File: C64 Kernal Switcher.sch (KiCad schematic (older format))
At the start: 11 parts, among them J1 Signals, J2 RGB, J3 LED, U1 2364, U2 PIC12F629-I/MS, U3 27C256

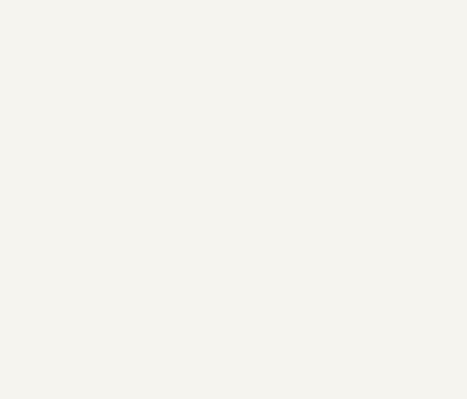
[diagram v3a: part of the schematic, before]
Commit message: Assigned footprints
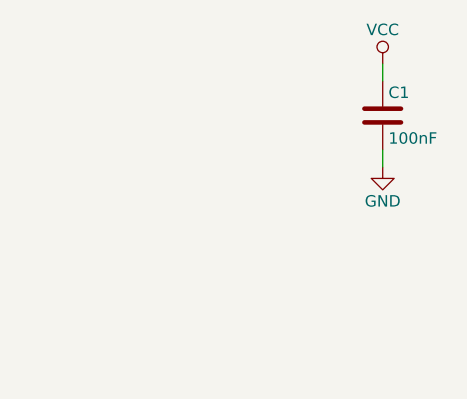
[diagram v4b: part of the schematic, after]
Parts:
- added C1: 100nF, Capacitors_THT:C_Disc_D4.7mm_W2.5mm_P5.00mm, symbol C
- J1: footprint (none) -> Pin_Headers:Pin_Header_Angled_1x02_Pitch2.54mm
- J2: footprint (none) -> Pin_Headers:Pin_Header_Straight_2x03_Pitch2.54mm
- U2: footprint (none) -> Housings_DIP:DIP-8_W7.62mm_Socket
- U3: footprint (none) -> Housings_DIP:DIP-28_W15.24mm_Socket_LongPads
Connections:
- net GND: now also C1.2
- net VCC: now also C1.1
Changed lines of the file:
@@
 	6075 2575 6175 2675
 $Comp
-L VCC #PWR01
+L VCC #PWR5
 U 1 1 5CC71BAE
 P 3900 3375
-F 0 "#PWR01" H 3900 3225 50  0001 C CNN
+F 0 "#PWR5" H 3900 3225 50  0001 C CNN
 F 1 "VCC" H 3900 3525 50  0000 C CNN
 F 2 "" H 3900 3375 50  0001 C CNN
@@
 CS
 $Comp
-L VCC #PWR02
+L VCC #PWR3
 U 1 1 5CC72126
 P 2700 1525
-F 0 "#PWR02" H 2700 1375 50  0001 C CNN
+F 0 "#PWR3" H 2700 1375 50  0001 C CNN
 F 1 "VCC" H 2700 1675 50  0000 C CNN
 F 2 "" H 2700 1525 50  0001 C CNN
@@
 $EndComp
 $Comp
-L GND #PWR03
+L GND #PWR4
 U 1 1 5CC72179
 P 2700 4025
-F 0 "#PWR03" H 2700 3775 50  0001 C CNN
+F 0 "#PWR4" H 2700 3775 50  0001 C CNN
 F 1 "GND" H 2700 3875 50  0000 C CNN
 F 2 "" H 2700 4025 50  0001 C CNN
@@
 $EndComp
 $Comp
-L VCC #PWR04
+L VCC #PWR8
 U 1 1 5CC72A38
 P 6875 1375
-F 0 "#PWR04" H 6875 1225 50  0001 C CNN
+F 0 "#PWR8" H 6875 1225 50  0001 C CNN
 F 1 "VCC" H 6875 1525 50  0000 C CNN
 F 2 "" H 6875 1375 50  0001 C CNN
@@
 $EndComp
 $Comp
-L GND #PWR05
+L GND #PWR9
 U 1 1 5CC72A4C
 P 6875 1875
-F 0 "#PWR05" H 6875 1625 50  0001 C CNN
+F 0 "#PWR9" H 6875 1625 50  0001 C CNN
 F 1 "GND" H 6875 1725 50  0000 C CNN
 F 2 "" H 6875 1875 50  0001 C CNN
@@
 $EndComp
 $Comp
-L VCC #PWR06
+L VCC #PWR10
 U 1 1 5CC72AB2
 P 7150 1950
-F 0 "#PWR06" H 7150 1800 50  0001 C CNN
+F 0 "#PWR10" H 7150 1800 50  0001 C CNN
 F 1 "VCC" H 7150 2100 50  0000 C CNN
 F 2 "" H 7150 1950 50  0001 C CNN
@@
 $EndComp
 $Comp
-L GND #PWR07
+L GND #PWR11
 U 1 1 5CC72AB8
 P 7150 2450
-F 0 "#PWR07" H 7150 2200 50  0001 C CNN
+F 0 "#PWR11" H 7150 2200 50  0001 C CNN
 F 1 "GND" H 7150 2300 50  0000 C CNN
 F 2 "" H 7150 2450 50  0001 C CNN
@@
 	6275 4950 6475 4950
 $Comp
-L GND #PWR08
+L GND #PWR7
 U 1 1 5CC74328
 P 6375 5050
-F 0 "#PWR08" H 6375 4800 50  0001 C CNN
+F 0 "#PWR7" H 6375 4800 50  0001 C CNN
 F 1 "GND" H 6375 4900 50  0000 C CNN
 F 2 "" H 6375 5050 50  0001 C CNN
@@
 F 0 "U2" H 2000 6300 50  0000 L CNN
 F 1 "PIC12F629-I/MS" H 2000 6200 50  0000 L CNN
-F 2 "" H 2550 5750 50  0001 C CNN
+F 2 "Housings_DIP:DIP-8_W7.62mm_Socket" H 2550 5750 50  0001 C CNN
 F 3 "" H 2550 5750 50  0001 C CNN
 	1    2550 5750
@@
 $EndComp
 $Comp
-L VCC #PWR09
+L VCC #PWR1
 U 1 1 5D07A987
 P 1775 5375
-F 0 "#PWR09" H 1775 5225 50  0001 C CNN
+F 0 "#PWR1" H 1775 5225 50  0001 C CNN
 F 1 "VCC" H 1775 5525 50  0000 C CNN
 F 2 "" H 1775 5375 50  0001 C CNN
@@
 	1775 5450 1850 5450
 $Comp
-L GND #PWR010
+L GND #PWR2
 U 1 1 5D07AAD6
 P 1775 6125
-F 0 "#PWR010" H 1775 5875 50  0001 C CNN
+F 0 "#PWR2" H 1775 5875 50  0001 C CNN
 F 1 "GND" H 1775 5975 50  0000 C CNN
 F 2 "" H 1775 6125 50  0001 C CNN
@@
 F 0 "U3" H 4975 3775 50  0000 C CNN
 F 1 "27C256" H 5125 1775 50  0000 C CNN
-F 2 "" H 5125 2775 50  0001 C CNN
+F 2 "Housings_DIP:DIP-28_W15.24mm_Socket_LongPads" H 5125 2775 50  0001 C CNN
 F 3 "" H 5125 2775 50  0001 C CNN
 	1    5125 2775
@@
 F 0 "J2" H 6675 5750 50  0000 C CNN
 F 1 "RGB" H 6675 5350 50  0000 C CNN
-F 2 "" H 6625 5550 50  0001 C CNN
+F 2 "Pin_Headers:Pin_Header_Straight_2x03_Pitch2.54mm" H 6625 5550 50  0001 C CNN
 F 3 "" H 6625 5550 50  0001 C CNN
 	1    6625 5550
@@
 NoConn ~ 6425 5650
 $Comp
-L GND #PWR011
+L GND #PWR12
 U 1 1 5D07DC30
 P 7350 5625
-F 0 "#PWR011" H 7350 5375 50  0001 C CNN
+F 0 "#PWR12" H 7350 5375 50  0001 C CNN
 F 1 "GND" H 7350 5475 50  0000 C CNN
 F 2 "" H 7350 5625 50  0001 C CNN
@@
 	7350 5550 6925 5550
 $Comp
-L GND #PWR012
+L GND #PWR6
 U 1 1 5D07DCBB
 P 6300 5625
-F 0 "#PWR012" H 6300 5375 50  0001 C CNN
+F 0 "#PWR6" H 6300 5375 50  0001 C CNN
 F 1 "GND" H 6300 5475 50  0000 C CNN
 F 2 "" H 6300 5625 50  0001 C CNN
@@
 F 0 "J1" H 6675 4275 50  0000 C CNN
 F 1 "Signals" H 6675 3975 50  0000 C CNN
-F 2 "" H 6675 4175 50  0001 C CNN
+F 2 "Pin_Headers:Pin_Header_Angled_1x02_Pitch2.54mm" H 6675 4175 50  0001 C CNN
 F 3 "" H 6675 4175 50  0001 C CNN
 	1    6675 4175
@@
 Text GLabel 6400 4275 0    60   BiDi ~ 0
 ~RESET
+$Comp
+L C C1
+U 1 1 5D07F04A
+P 10300 950
+F 0 "C1" H 10325 1050 50  0000 L CNN
+F 1 "100nF" H 10325 850 50  0000 L CNN
+F 2 "Capacitors_THT:C_Disc_D4.7mm_W2.5mm_P5.00mm" H 10338 800 50  0001 C CNN
+F 3 "" H 10300 950 50  0001 C CNN
+	1    10300 950
+	1    0    0    -1
+$EndComp
+$Comp
+L VCC #PWR13
+U 1 1 5D07F12B
+P 10300 725
+F 0 "#PWR13" H 10300 575 50  0001 C CNN
+F 1 "VCC" H 10300 875 50  0000 C CNN
+F 2 "" H 10300 725 50  0001 C CNN
+F 3 "" H 10300 725 50  0001 C CNN
+	1    10300 725
+	1    0    0    -1
+$EndComp
+$Comp
+L GND #PWR14
+U 1 1 5D07F1EA
+P 10300 1175
+F 0 "#PWR14" H 10300 925 50  0001 C CNN
+F 1 "GND" H 10300 1025 50  0000 C CNN
+F 2 "" H 10300 1175 50  0001 C CNN
+F 3 "" H 10300 1175 50  0001 C CNN
+	1    10300 1175
+	1    0    0    -1
+$EndComp
+Wire Wire Line
+	10300 1175 10300 1100
+Wire Wire Line
+	10300 800  10300 725
 $EndSCHEMATC

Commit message: Layout redone
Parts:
- J3: footprint Pin_Headers:Pin_Header_Straight_1x03_Pitch2.54mm -> Pin_Headers:Pin_Header_Angled_1x03_Pitch2.54mm
- U1: footprint Housings_DIP:DIP-24_W15.24mm_Socket -> 2364:DIP-24_W15.24mm_Socket
- U3: footprint Housings_DIP:DIP-28_W15.24mm_Socket_LongPads -> Housings_DIP:DIP-28_W15.24mm_Socket
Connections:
- net CS: no longer U3.20 (CE)
- net GND: now also U3.20 (CE)
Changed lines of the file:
@@
 F 0 "U1" H 2900 3775 50  0000 C CNN
 F 1 "2364" H 3000 1775 50  0000 C CNN
-F 2 "Housings_DIP:DIP-24_W15.24mm_Socket" H 2700 2775 50  0001 C CNN
+F 2 "2364:DIP-24_W15.24mm_Socket" H 2700 2775 50  0001 C CNN
 F 3 "" H 2700 2775 50  0001 C CNN
 	1    2700 2775
@@
 	4075 2975 4175 3075
 Entry Wire Line
-	4075 3475 4175 3575
+	4075 3575 4175 3675
 Text Label 4400 3175 2    60   ~ 0
 A13
@@
 	6075 2575 6175 2675
 $Comp
-L VCC #PWR5
+L VCC #PWR01
 U 1 1 5CC71BAE
 P 3900 3375
-F 0 "#PWR5" H 3900 3225 50  0001 C CNN
+F 0 "#PWR01" H 3900 3225 50  0001 C CNN
 F 1 "VCC" H 3900 3525 50  0000 C CNN
 F 2 "" H 3900 3375 50  0001 C CNN
@@
 Text Label 1975 3675 2    60   ~ 0
 CS
-Text Label 4200 3575 0    60   ~ 0
+Text Label 4225 3675 0    60   ~ 0
 CS
 $Comp
-L VCC #PWR3
+L VCC #PWR02
 U 1 1 5CC72126
 P 2700 1525
-F 0 "#PWR3" H 2700 1375 50  0001 C CNN
+F 0 "#PWR02" H 2700 1375 50  0001 C CNN
 F 1 "VCC" H 2700 1675 50  0000 C CNN
 F 2 "" H 2700 1525 50  0001 C CNN
@@
 $EndComp
 $Comp
-L GND #PWR4
+L GND #PWR03
 U 1 1 5CC72179
 P 2700 4025
-F 0 "#PWR4" H 2700 3775 50  0001 C CNN
+F 0 "#PWR03" H 2700 3775 50  0001 C CNN
 F 1 "GND" H 2700 3875 50  0000 C CNN
 F 2 "" H 2700 4025 50  0001 C CNN
@@
 $EndComp
 $Comp
-L VCC #PWR8
+L VCC #PWR04
 U 1 1 5CC72A38
 P 6875 1375
-F 0 "#PWR8" H 6875 1225 50  0001 C CNN
+F 0 "#PWR04" H 6875 1225 50  0001 C CNN
 F 1 "VCC" H 6875 1525 50  0000 C CNN
 F 2 "" H 6875 1375 50  0001 C CNN
@@
 $EndComp
 $Comp
-L GND #PWR9
+L GND #PWR05
 U 1 1 5CC72A4C
 P 6875 1875
-F 0 "#PWR9" H 6875 1625 50  0001 C CNN
+F 0 "#PWR05" H 6875 1625 50  0001 C CNN
 F 1 "GND" H 6875 1725 50  0000 C CNN
 F 2 "" H 6875 1875 50  0001 C CNN
@@
 $EndComp
 $Comp
-L VCC #PWR10
+L VCC #PWR06
 U 1 1 5CC72AB2
 P 7150 1950
-F 0 "#PWR10" H 7150 1800 50  0001 C CNN
+F 0 "#PWR06" H 7150 1800 50  0001 C CNN
 F 1 "VCC" H 7150 2100 50  0000 C CNN
 F 2 "" H 7150 1950 50  0001 C CNN
@@
 $EndComp
 $Comp
-L GND #PWR11
+L GND #PWR07
 U 1 1 5CC72AB8
 P 7150 2450
-F 0 "#PWR11" H 7150 2200 50  0001 C CNN
+F 0 "#PWR07" H 7150 2200 50  0001 C CNN
 F 1 "GND" H 7150 2300 50  0000 C CNN
 F 2 "" H 7150 2450 50  0001 C CNN
@@
 Wire Wire Line
 	4175 3075 4425 3075
-Wire Wire Line
-	4175 3575 4425 3575
 Wire Wire Line
 	4175 3175 4425 3175
@@
 	3750 1050 3750 2675
 Wire Bus Line
-	4075 1050 4075 3475
+	4075 1050 4075 3575
 Wire Bus Line
 	6175 1050 6175 2675
@@
 	6275 2200 7050 2200
 Wire Wire Line
-	4425 3675 4350 3675
-Wire Wire Line
-	4350 3675 4350 3575
-Connection ~ 4350 3575
+	4175 3675 4425 3675
 Text GLabel 6650 1700 3    60   Input ~ 0
 A13
@@
 	6275 4950 6475 4950
 $Comp
-L GND #PWR7
+L GND #PWR08
 U 1 1 5CC74328
 P 6375 5050
-F 0 "#PWR7" H 6375 4800 50  0001 C CNN
+F 0 "#PWR08" H 6375 4800 50  0001 C CNN
 F 1 "GND" H 6375 4900 50  0000 C CNN
 F 2 "" H 6375 5050 50  0001 C CNN
@@
 F 0 "J3" H 6675 5050 50  0000 C CNN
 F 1 "LED" H 6675 4650 50  0000 C CNN
-F 2 "Pin_Headers:Pin_Header_Straight_1x03_Pitch2.54mm" H 6675 4850 50  0001 C CNN
+F 2 "Pin_Headers:Pin_Header_Angled_1x03_Pitch2.54mm" H 6675 4850 50  0001 C CNN
 F 3 "" H 6675 4850 50  0001 C CNN
 	1    6675 4850
@@
 $EndComp
 $Comp
-L VCC #PWR1
+L VCC #PWR09
 U 1 1 5D07A987
 P 1775 5375
-F 0 "#PWR1" H 1775 5225 50  0001 C CNN
+F 0 "#PWR09" H 1775 5225 50  0001 C CNN
 F 1 "VCC" H 1775 5525 50  0000 C CNN
 F 2 "" H 1775 5375 50  0001 C CNN
@@
 	1775 5450 1850 5450
 $Comp
-L GND #PWR2
+L GND #PWR010
 U 1 1 5D07AAD6
 P 1775 6125
-F 0 "#PWR2" H 1775 5875 50  0001 C CNN
+F 0 "#PWR010" H 1775 5875 50  0001 C CNN
 F 1 "GND" H 1775 5975 50  0000 C CNN
 F 2 "" H 1775 6125 50  0001 C CNN
@@
 F 0 "U3" H 4975 3775 50  0000 C CNN
 F 1 "27C256" H 5125 1775 50  0000 C CNN
-F 2 "Housings_DIP:DIP-28_W15.24mm_Socket_LongPads" H 5125 2775 50  0001 C CNN
+F 2 "Housings_DIP:DIP-28_W15.24mm_Socket" H 5125 2775 50  0001 C CNN
 F 3 "" H 5125 2775 50  0001 C CNN
 	1    5125 2775
@@
 NoConn ~ 6425 5650
 $Comp
-L GND #PWR12
+L GND #PWR011
 U 1 1 5D07DC30
 P 7350 5625
-F 0 "#PWR12" H 7350 5375 50  0001 C CNN
+F 0 "#PWR011" H 7350 5375 50  0001 C CNN
 F 1 "GND" H 7350 5475 50  0000 C CNN
 F 2 "" H 7350 5625 50  0001 C CNN
@@
 	7350 5550 6925 5550
 $Comp
-L GND #PWR6
+L GND #PWR012
 U 1 1 5D07DCBB
 P 6300 5625
-F 0 "#PWR6" H 6300 5375 50  0001 C CNN
+F 0 "#PWR012" H 6300 5375 50  0001 C CNN
 F 1 "GND" H 6300 5475 50  0000 C CNN
 F 2 "" H 6300 5625 50  0001 C CNN
@@
 $EndComp
 $Comp
-L VCC #PWR13
+L VCC #PWR013
 U 1 1 5D07F12B
 P 10300 725
-F 0 "#PWR13" H 10300 575 50  0001 C CNN
+F 0 "#PWR013" H 10300 575 50  0001 C CNN
 F 1 "VCC" H 10300 875 50  0000 C CNN
 F 2 "" H 10300 725 50  0001 C CNN
@@
 $EndComp
 $Comp
-L GND #PWR14
+L GND #PWR014
 U 1 1 5D07F1EA
 P 10300 1175
-F 0 "#PWR14" H 10300 925 50  0001 C CNN
+F 0 "#PWR014" H 10300 925 50  0001 C CNN
 F 1 "GND" H 10300 1025 50  0000 C CNN
 F 2 "" H 10300 1175 50  0001 C CNN
@@
 Wire Wire Line
 	10300 800  10300 725
+$Comp
+L GND #PWR?
+U 1 1 5D07DD0A
+P 3900 3500
+F 0 "#PWR?" H 3900 3250 50  0001 C CNN
+F 1 "GND" H 3900 3350 50  0000 C CNN
+F 2 "" H 3900 3500 50  0001 C CNN
+F 3 "" H 3900 3500 50  0001 C CNN
+	1    3900 3500
+	1    0    0    -1
+$EndComp
+Wire Wire Line
+	3900 3425 3900 3500
+Wire Wire Line
+	3900 3425 4350 3425
+Wire Wire Line
+	4350 3425 4350 3575
+Wire Wire Line
+	4350 3575 4425 3575
 $EndSCHEMATC

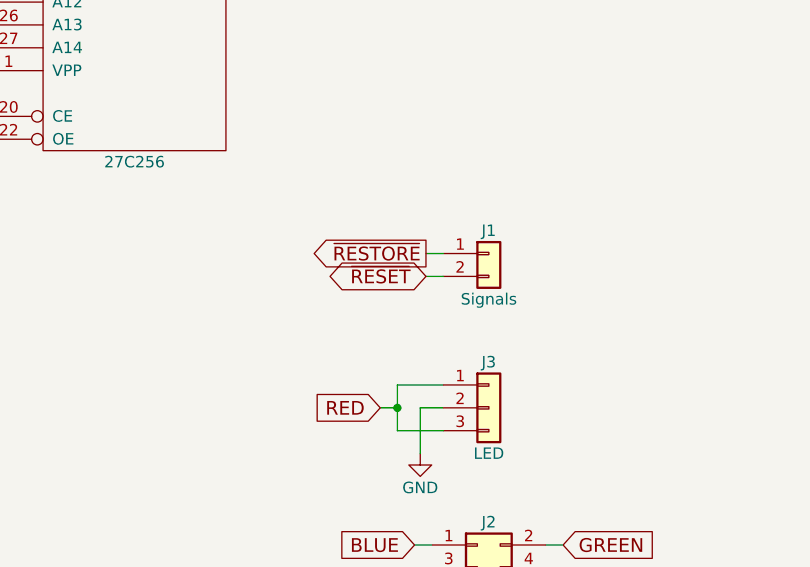
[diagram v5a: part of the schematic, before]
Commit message: Updated silkscreen
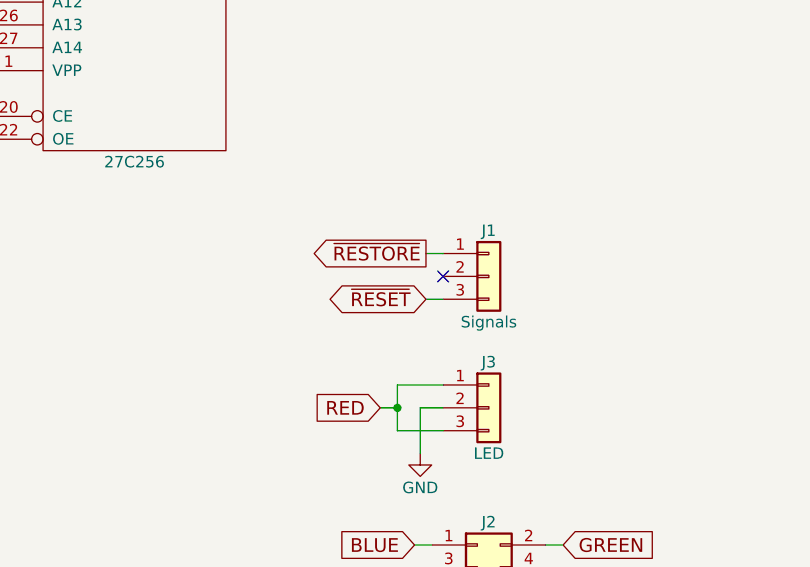
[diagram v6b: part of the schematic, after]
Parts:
- removed J1: Signals, Pin_Headers:Pin_Header_Angled_1x02_Pitch2.54mm, symbol Conn_01x02
- added J1: Signals, Pin_Headers:Pin_Header_Angled_1x03_Pitch2.54mm, symbol Conn_01x03
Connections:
- net ~RESET: now also J1.3 (Pin_3)
- net ~RESTORE: now also J1.1 (Pin_1)
- no-connect marks 2 -> 3
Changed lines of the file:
@@
 Wire Wire Line
 	7350 5550 7350 5625
-$Comp
-L Conn_01x02 J1
-U 1 1 5D07E10A
-P 6675 4175
-F 0 "J1" H 6675 4275 50  0000 C CNN
-F 1 "Signals" H 6675 3975 50  0000 C CNN
-F 2 "Pin_Headers:Pin_Header_Angled_1x02_Pitch2.54mm" H 6675 4175 50  0001 C CNN
-F 3 "" H 6675 4175 50  0001 C CNN
-	1    6675 4175
-	1    0    0    -1
-$EndComp
 Text GLabel 6400 4175 0    60   Output ~ 0
 ~RESTORE
@@
 	6400 4175 6475 4175
 Wire Wire Line
-	6400 4275 6475 4275
-Text GLabel 6400 4275 0    60   BiDi ~ 0
+	6400 4375 6475 4375
+Text GLabel 6400 4375 0    60   BiDi ~ 0
 ~RESET
 $Comp
@@
 Wire Wire Line
 	4350 3575 4425 3575
+$Comp
+L Conn_01x03 J1
+U 1 1 5D07EA73
+P 6675 4275
+F 0 "J1" H 6675 4475 50  0000 C CNN
+F 1 "Signals" H 6675 4075 50  0000 C CNN
+F 2 "Pin_Headers:Pin_Header_Angled_1x03_Pitch2.54mm" H 6675 4275 50  0001 C CNN
+F 3 "" H 6675 4275 50  0001 C CNN
+	1    6675 4275
+	1    0    0    -1
+$EndComp
+NoConn ~ 6475 4275
 $EndSCHEMATC

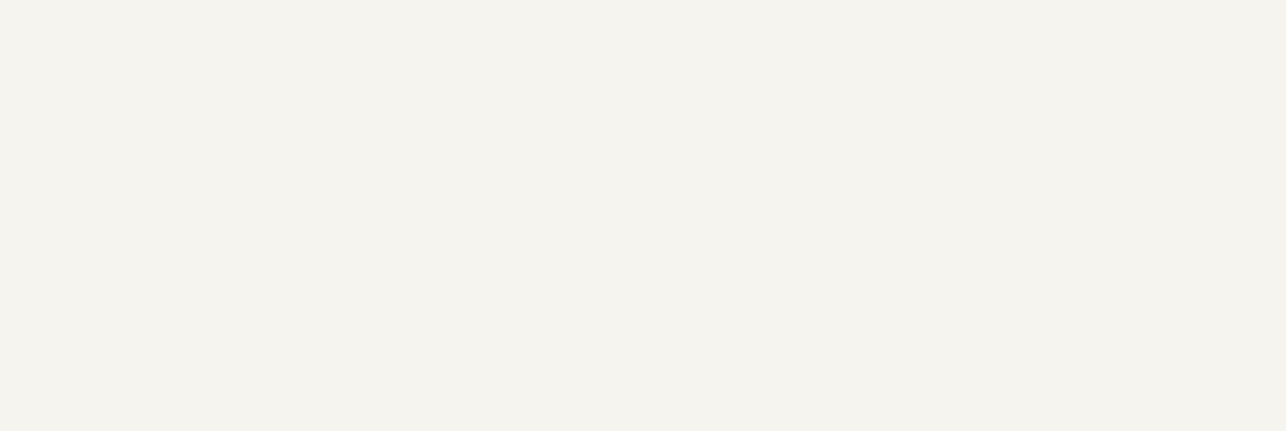
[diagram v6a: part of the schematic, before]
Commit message: Moved R1 so it fits better under socket
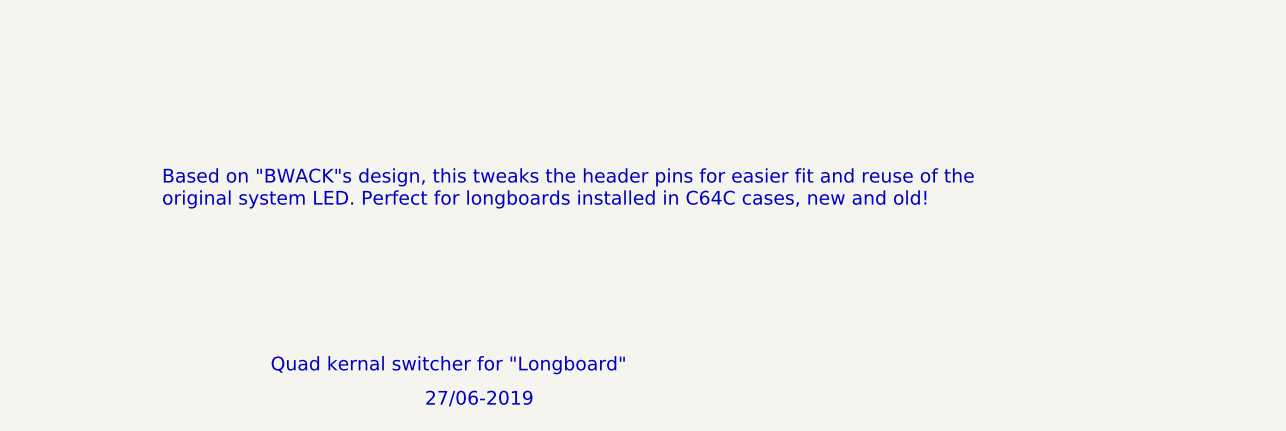
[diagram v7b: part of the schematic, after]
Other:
- note added: "27/06-2019"
- note added: "Based on "BWACK"s design, this tweaks the header pins for easier fit and reuse of the\noriginal system LED. Perfect for longboards installed in C64C cases, new and old!"
- note added: "Quad kernal switcher for "Longboard""
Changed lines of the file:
@@
 $EndComp
 NoConn ~ 6475 4275
+Text Notes 7475 7500 0    60   ~ 0
+Quad kernal switcher for "Longboard"
+Text Notes 7000 6775 0    60   ~ 0
+Based on "BWACK"s design, this tweaks the header pins for easier fit and reuse of the\noriginal system LED. Perfect for longboards installed in C64C cases, new and old!
+Text Notes 8150 7650 0    60   ~ 0
+27/06-2019
 $EndSCHEMATC
